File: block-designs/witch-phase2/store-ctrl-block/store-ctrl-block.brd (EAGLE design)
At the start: 27.9 x 27.9 mm, 19 parts, among them IC1 74LVC1G125DBV, IC2 74LVC1G125DBV, Q1 MMBT2907ALT1SMD, Q2 MMBT2907ALT1SMD

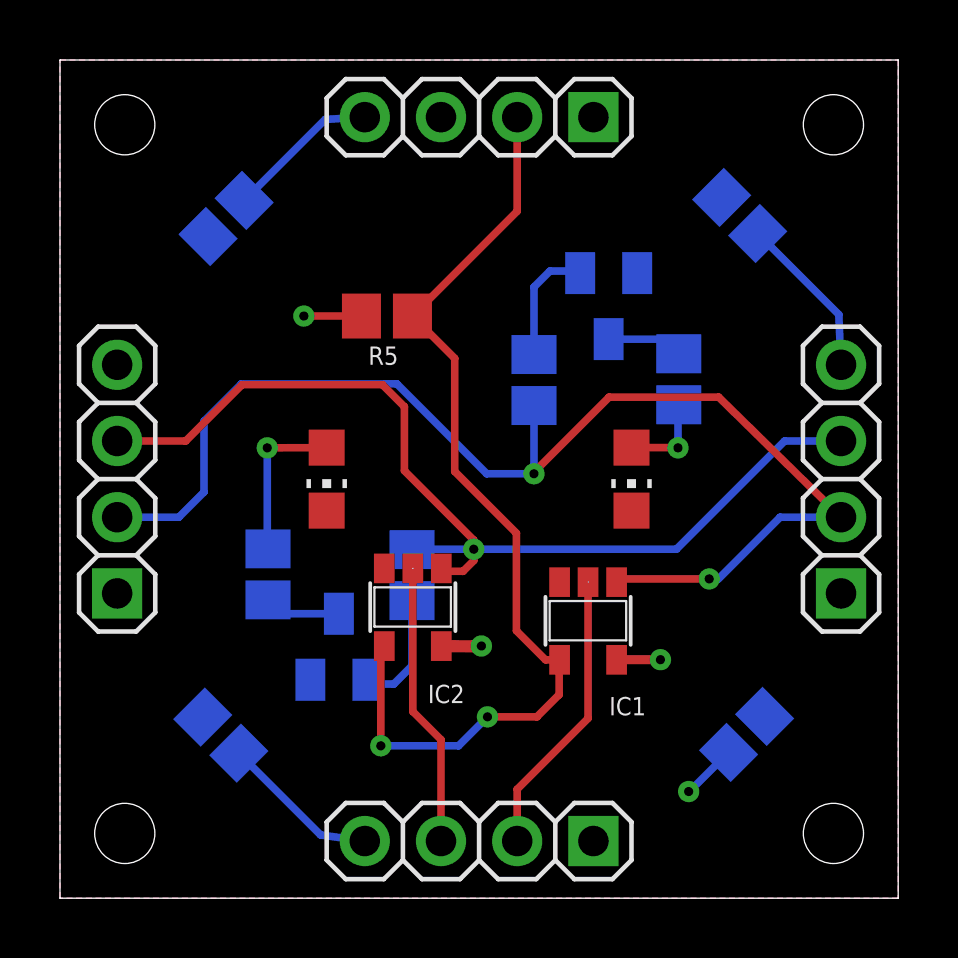
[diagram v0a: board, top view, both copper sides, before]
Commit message: adjust borders for ground/vcc plains and size to match 1.1inch grids
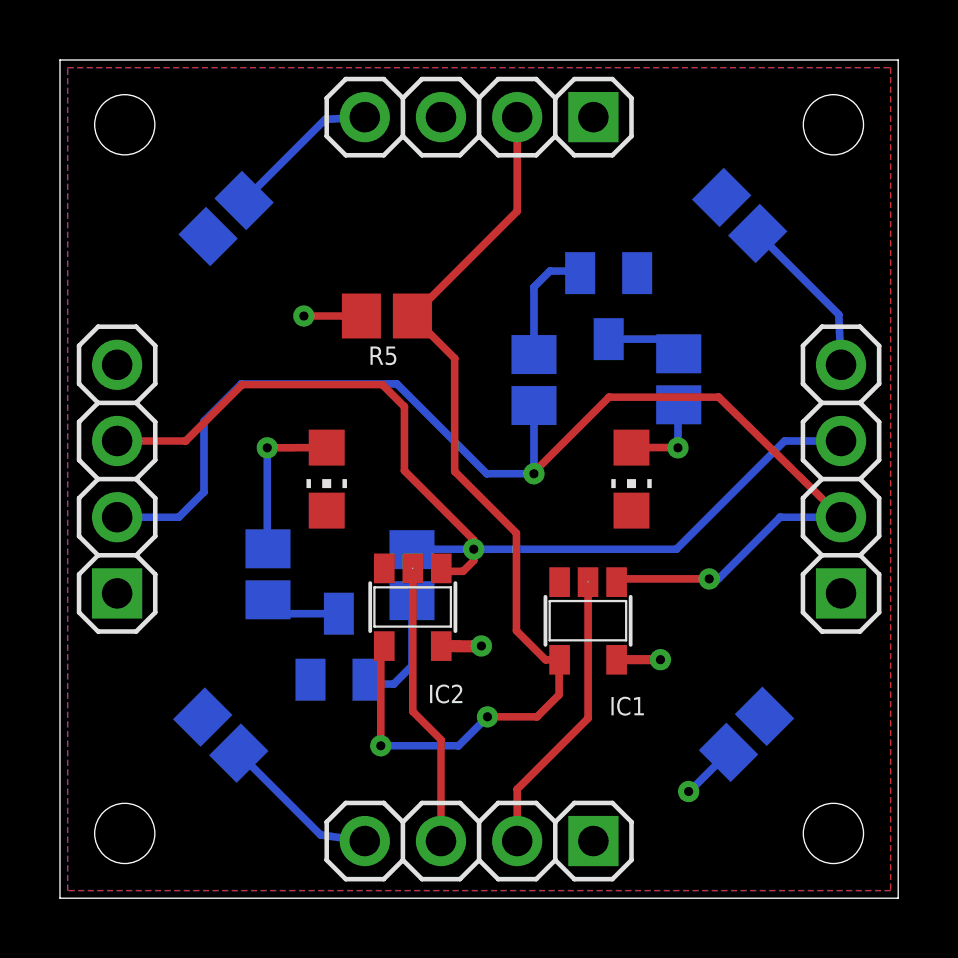
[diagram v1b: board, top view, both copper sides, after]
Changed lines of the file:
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@@
 <contactref element="C4" pad="2"/>
 <contactref element="JP2" pad="4"/>
-<polygon width="0" layer="1">
-<vertex x="27.94" y="0"/>
-<vertex x="0" y="0"/>
-<vertex x="0" y="27.94"/>
-<vertex x="27.94" y="27.94"/>
+<polygon width="0.254" layer="1">
+<vertex x="27.686" y="0.254"/>
+<vertex x="0.254" y="0.254"/>
+<vertex x="0.254" y="27.686"/>
+<vertex x="27.686" y="27.686"/>
 </polygon>
 <contactref element="JP1" pad="4"/>
@@
 <contactref element="C4" pad="1"/>
 <contactref element="JP2" pad="1"/>
-<polygon width="0" layer="16">
-<vertex x="27.94" y="0"/>
-<vertex x="0" y="0"/>
-<vertex x="0" y="27.94"/>
-<vertex x="27.94" y="27.94"/>
+<polygon width="0.254" layer="16">
+<vertex x="27.686" y="0.254"/>
+<vertex x="0.254" y="0.254"/>
+<vertex x="0.254" y="27.686"/>
+<vertex x="27.686" y="27.686"/>
 </polygon>
 <contactref element="JP1" pad="1"/>

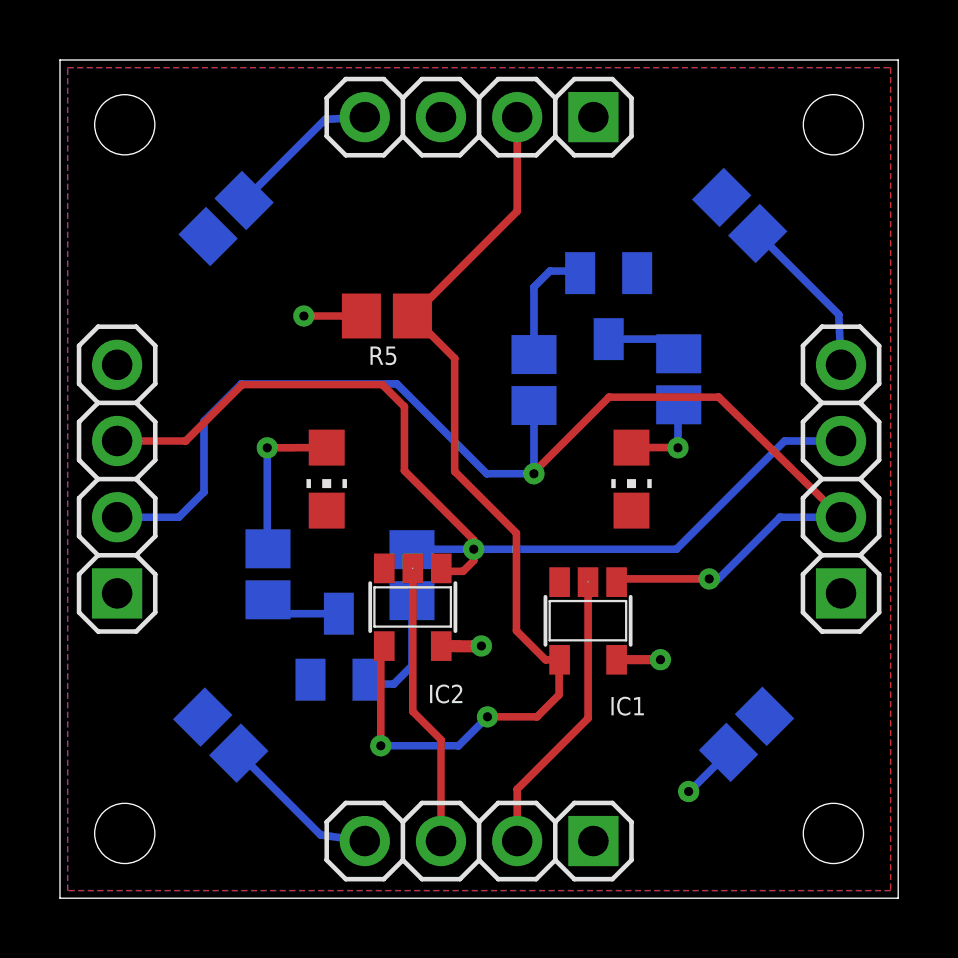
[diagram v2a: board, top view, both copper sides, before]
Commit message: updated designs for new labeling and spacing
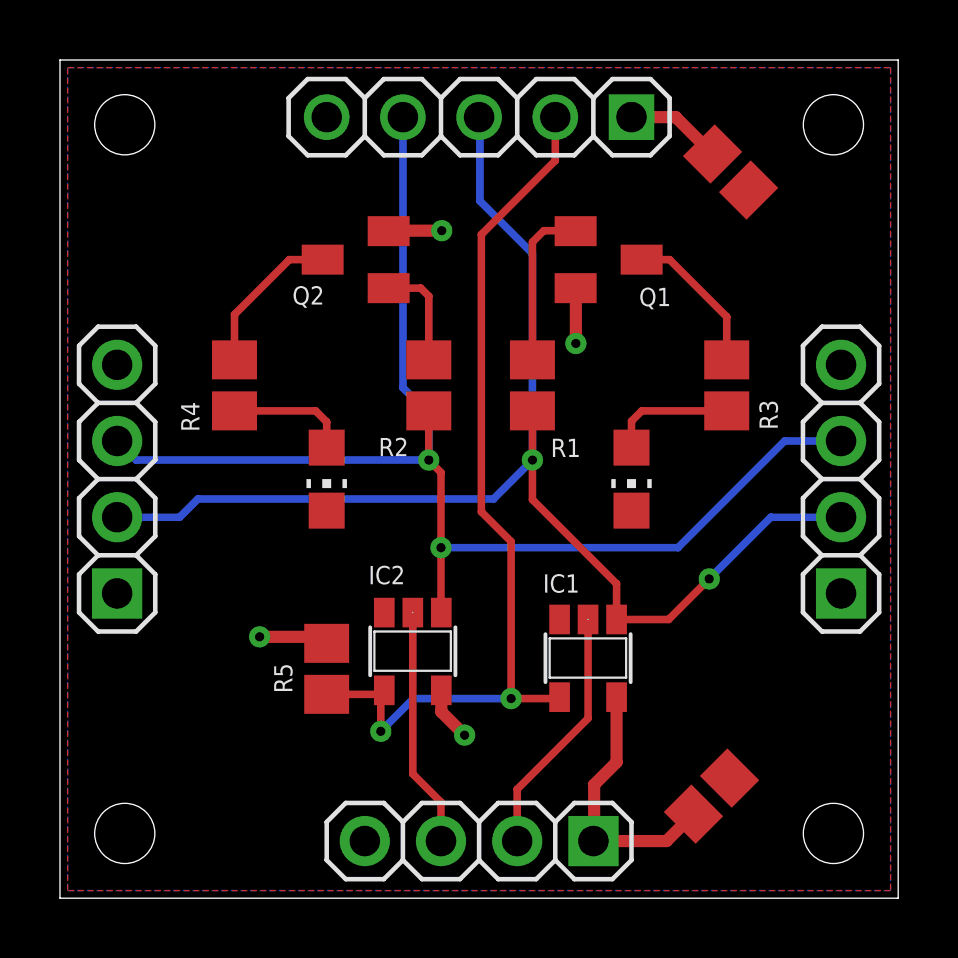
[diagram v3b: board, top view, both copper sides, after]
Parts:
- removed C3, C4: (no value), resistor:C0805
- C1, C2: value (none) -> 10uF
- JP2: device pinhead:1X04 -> pinhead:1X05
- R1, R2: value (none) -> 1K
- R3, R4: value (none) -> 270
- R5: value (none) -> 100K
- moved C2 25.3 mm to (22.4, 24.2), flipped to the top, turned to 315 degrees
- moved Q2 12.9 mm to (9.86, 21.3), flipped to the top, turned to 90 degrees
- moved R5 11.9 mm to (8.89, 7.65), turned to 90 degrees
- moved R4 6.40 mm to (5.82, 17.1), flipped to the top, turned to 270 degrees
- moved R2 6.35 mm to (12.3, 17.1), flipped to the top, turned to 270 degrees
- moved C1 2.37 mm to (21.7, 3.40), flipped to the top, turned to 45 degrees
- moved R3 1.61 mm to (22.2, 17.1), flipped to the top
- moved Q1 1.55 mm to (18.3, 21.3), flipped to the top, turned to 270 degrees
- moved IC2 1.47 mm to (11.8, 8.23)
- moved IC1 1.24 mm to (17.6, 8.00)
- moved R1 0.18 mm to (15.7, 17.1), flipped to the top
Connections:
- removed net +5V: C1.1, C2.1, C3.1, C4.1, IC1.5, IC2.5, JP1.1, JP2.1, JP3.1, JP4.1, Q1.E, Q2.E, R5.2
- new net VCC: C1.1, C2.1, IC1.5, IC2.5, JP1.1, JP2.1, JP3.1, JP4.1, Q1.E, Q2.E, R5.2
- net GND: now also JP2.5; no longer C3.2, C4.2, JP2.4
- net RCV_EN: now also JP2.4
- net SND_EN: now also JP2.3
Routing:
- net VCC: track 0.00 -> 19.9 mm, vias 0 -> 4
- net GND: track 17.9 -> 0.00 mm, vias 1 -> 0
- net RCV_EN: track 33.8 -> 44.3 mm, vias 1 -> 2
- net +5V: track 4.72 -> 0.00 mm, vias 3 -> 0
- net N$3: track 2.55 -> 5.21 mm
- net SND_RCV: track 33.0 -> 30.5 mm
- net N$4: track 2.54 -> 5.06 mm
- net SND_EN: track 42.0 -> 43.8 mm
- net N$2: track 4.04 -> 5.53 mm
- net RCV_ROW: track 9.48 -> 8.00 mm
- net N$6: track 5.36 -> 4.08 mm, vias 1 -> 0
- net SND_ROW: track 9.61 -> 8.36 mm
- net N$5: track 3.04 -> 4.20 mm, vias 1 -> 0
- added copper zone on layer 16, net VCC
- removed copper zone on layer 16, net +5V
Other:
- board text removed: "TOP"
